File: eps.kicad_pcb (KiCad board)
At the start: 4 copper layers, 95.9 x 90.2 mm, 185 parts, among them J1 PC104-8BIT, J2 PC104PTH, J3 PC104PTH, J4 PC104PTH, J5 PC104PTH, P1 3pin-DC-power, P2 3pin-DC-power, Q10 CSD17551Q3A, Q11 CSD17551Q3A, Q12 CSD17551Q3A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

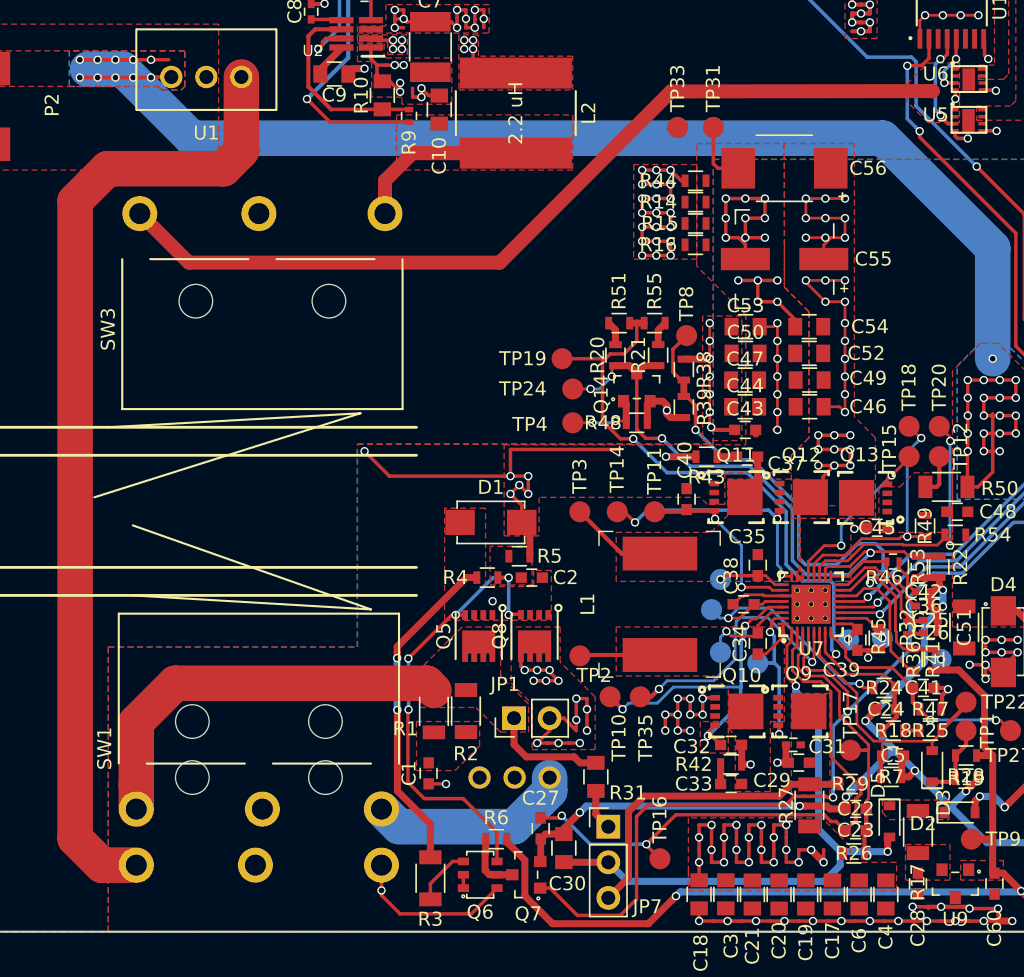
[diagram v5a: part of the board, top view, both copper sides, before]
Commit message: Fix switch footprint terminal spacing and adjust track ends accordingly
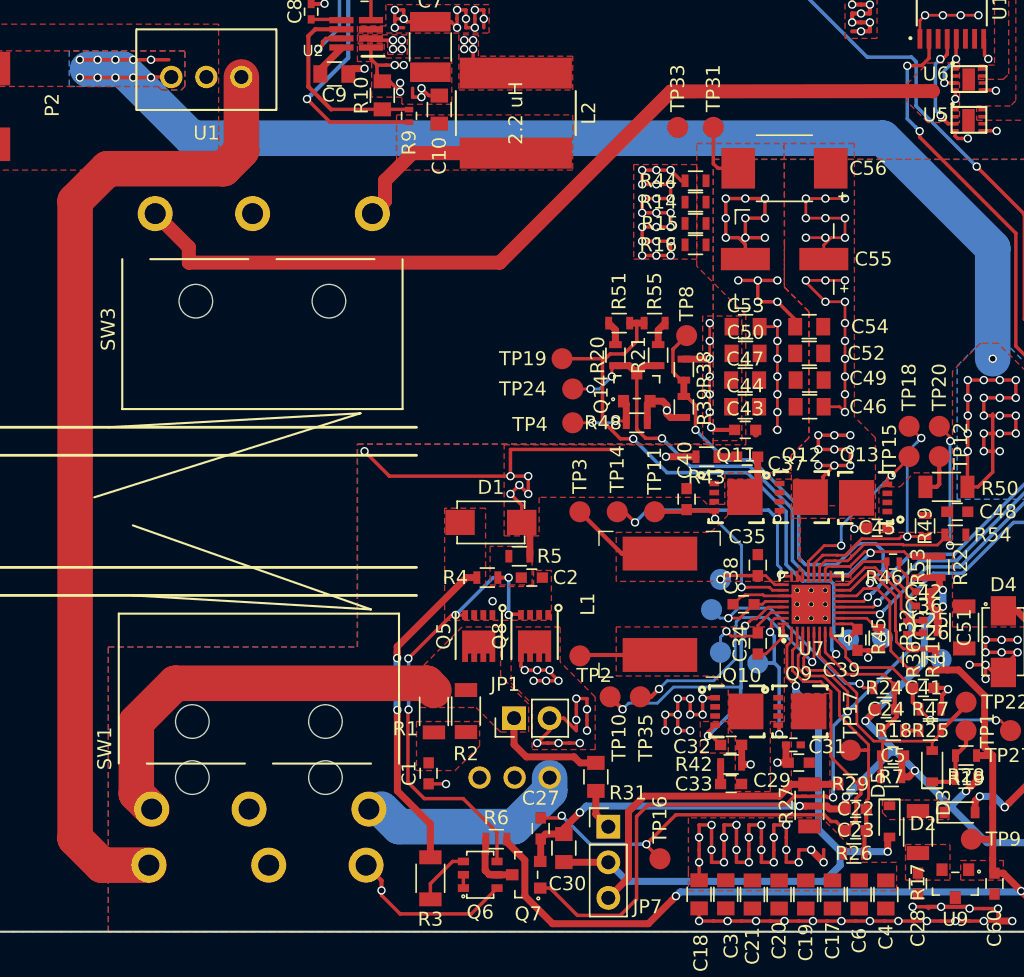
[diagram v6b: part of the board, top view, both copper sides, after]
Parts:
- SW1: footprint SFUSat:SS-3GLPD-L -> SS-3GLPD-L
- SW3: footprint SFUSat:SS-3GLPD-R -> SS-3GLPD-R
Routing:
- net GNDPWR: track 151.5 -> 150.2 mm
- net /return: track 69.3 -> 70.2 mm

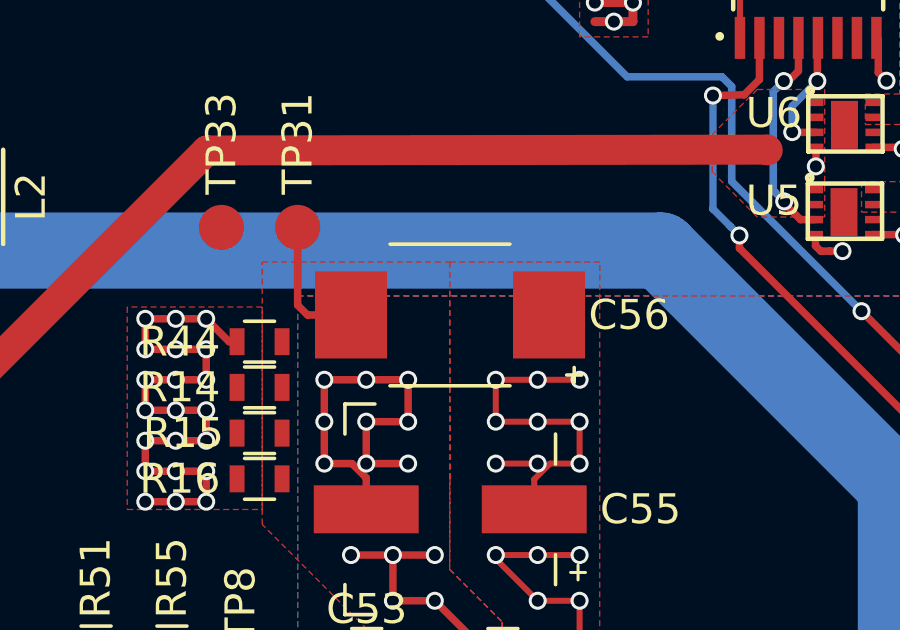
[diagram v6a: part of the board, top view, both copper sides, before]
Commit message: Move pads closer together on C56 footprint
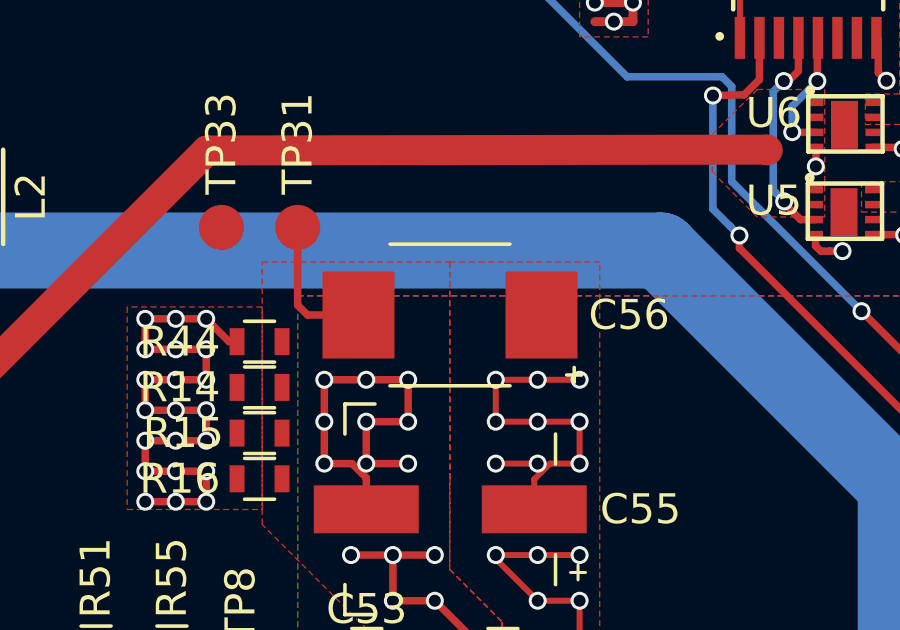
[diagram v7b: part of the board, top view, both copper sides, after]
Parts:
- C56: footprint SFUSat-cap:C_TANT_2917 -> C_TANT_2917
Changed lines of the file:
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@@
     (uvia_drill 0.1)
+  )
+  (module C_TANT_2917 (layer F.Cu)
+    (at 169.26 80.517 180)
+    (fp_text reference C56 (at -5.971 0 180) (layer F.SilkS)
+      (effects (font (size 1 1) (thickness 0.15)))
+    )
+    (fp_text value 47u (at 0 3.5 180) (layer F.Fab)
+      (effects (font (size 1 1) (thickness 0.15)))
+    )
+    (fp_text user REF** (at 0 -3.5 180) (layer F.Fab)
+      (effects (font (size 1 1) (thickness 0.15)))
+    )
+    (fp_line (start 4.525 2.435) (end 4.525 -2.435) (layer F.CrtYd) (width 0.05))
+    (fp_line (start 4.525 -2.435) (end -4.525 -2.435) (layer F.CrtYd) (width 0.05))
+    (fp_line (start -4.525 -2.435) (end -4.525 2.435) (layer F.CrtYd) (width 0.05))
+    (fp_line (start -4.525 2.435) (end 4.525 2.435) (layer F.CrtYd) (width 0.05))
+    (fp_line (start -4.14 -2.25) (end -4.14 -1.75) (layer F.SilkS) (width 0.12))
+    (fp_line (start -3.89 -2) (end -4.39 -2) (layer F.SilkS) (width 0.12))
+    (fp_line (start -2 2.36) (end 2 2.36) (layer F.SilkS) (width 0.12))
+    (fp_line (start -2 -2.36) (end 2 -2.36) (layer F.SilkS) (width 0.12))
+    (fp_line (start -3.75 -2.25) (end -3.75 2.25) (layer F.Fab) (width 0.1))
+    (fp_line (start -3.75 2.25) (end 3.75 2.25) (layer F.Fab) (width 0.1))
+    (fp_line (start 3.75 2.25) (end 3.75 -2.25) (layer F.Fab) (width 0.1))
+    (fp_line (start 3.75 -2.25) (end -3.75 -2.25) (layer F.Fab) (width 0.1))
+    (pad 1 smd rect (at -3.05 0 180) (size 2.4 2.9) (layers F.Cu F.Paste F.Mask)
+      (net 104 /VSYS_UP))
+    (pad 2 smd rect (at 3.05 0 180) (size 2.4 2.9) (layers F.Cu F.Paste F.Mask)
+      (net 44 GNDPWR))
   )
   (module SFUSat:SS-3GLPD-L (layer B.Cu)
@@
     )
   )
-  (module SFUSat-cap:C_TANT_2917 (layer F.Cu)
-    (at 169.26 80.517 180)
-    (fp_text reference C56 (at -5.971 0 180) (layer F.SilkS)
-      (effects (font (size 1 1) (thickness 0.15)))
-    )
-    (fp_text value 47u (at 0 3.5 180) (layer F.Fab)
-      (effects (font (size 1 1) (thickness 0.15)))
-    )
-    (fp_text user REF** (at 0 -3.5 180) (layer F.Fab)
-      (effects (font (size 1 1) (thickness 0.15)))
-    )
-    (fp_line (start 4.525 2.435) (end 4.525 -2.435) (layer F.CrtYd) (width 0.05))
-    (fp_line (start 4.525 -2.435) (end -4.525 -2.435) (layer F.CrtYd) (width 0.05))
-    (fp_line (start -4.525 -2.435) (end -4.525 2.435) (layer F.CrtYd) (width 0.05))
-    (fp_line (start -4.525 2.435) (end 4.525 2.435) (layer F.CrtYd) (width 0.05))
-    (fp_line (start -4.14 -2.25) (end -4.14 -1.75) (layer F.SilkS) (width 0.12))
-    (fp_line (start -3.89 -2) (end -4.39 -2) (layer F.SilkS) (width 0.12))
-    (fp_line (start -2 2.36) (end 2 2.36) (layer F.SilkS) (width 0.12))
-    (fp_line (start -2 -2.36) (end 2 -2.36) (layer F.SilkS) (width 0.12))
-    (fp_line (start -3.75 -2.25) (end -3.75 2.25) (layer F.Fab) (width 0.1))
-    (fp_line (start -3.75 2.25) (end 3.75 2.25) (layer F.Fab) (width 0.1))
-    (fp_line (start 3.75 2.25) (end 3.75 -2.25) (layer F.Fab) (width 0.1))
-    (fp_line (start 3.75 -2.25) (end -3.75 -2.25) (layer F.Fab) (width 0.1))
-    (pad 1 smd rect (at -3.3 0 180) (size 2.4 2.9) (layers F.Cu F.Paste F.Mask)
-      (net 104 /VSYS_UP))
-    (pad 2 smd rect (at 3.3 0 180) (size 2.4 2.9) (layers F.Cu F.Paste F.Mask)
-      (net 44 GNDPWR))
-  )
   (module SFUSat:B3B-XH-A (layer F.Cu)

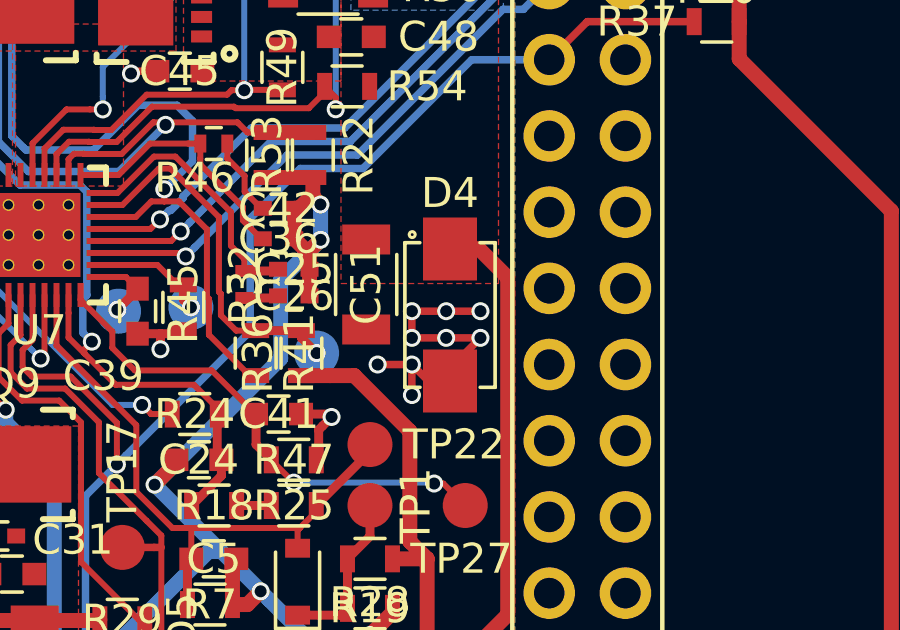
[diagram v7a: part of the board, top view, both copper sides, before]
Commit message: Update D4 pad dimensions and spacing to patch datasheet, regenerate pours
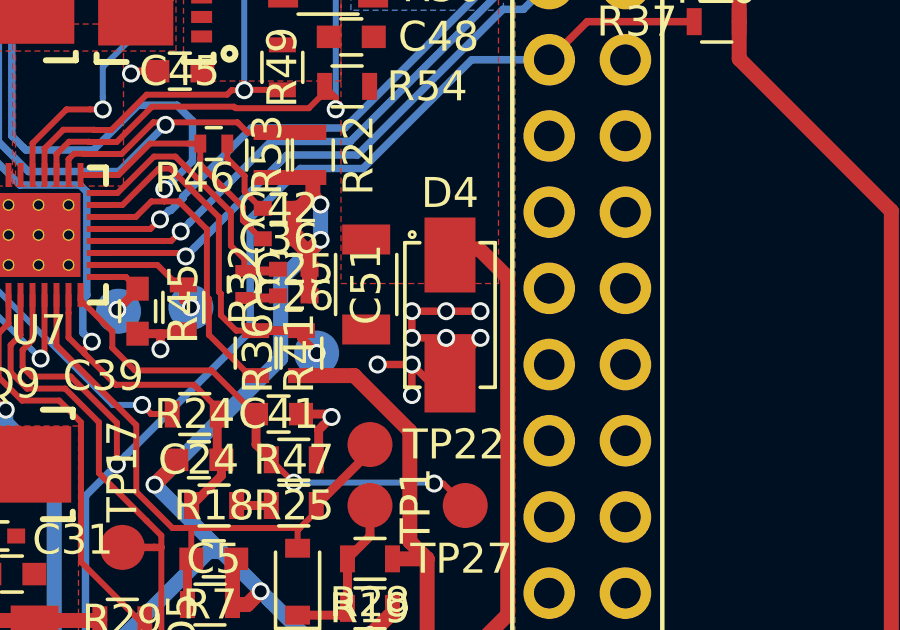
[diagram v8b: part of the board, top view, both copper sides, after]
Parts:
- D4: footprint SFUSat:DO-214AC -> DO-214AC
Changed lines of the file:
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@@
     (31 B.Cu signal hide)
     (33 F.Adhes user hide)
-    (35 F.Paste user hide)
+    (35 F.Paste user)
     (36 B.SilkS user)
     (37 F.SilkS user)
     (38 B.Mask user)
     (39 F.Mask user)
-    (40 Dwgs.User user hide)
-    (41 Cmts.User user hide)
+    (40 Dwgs.User user)
+    (41 Cmts.User user)
     (42 Eco1.User user hide)
-    (43 Eco2.User user hide)
+    (43 Eco2.User user)
     (44 Edge.Cuts user)
     (45 Margin user hide)
@@
     (uvia_drill 0.1)
   )
+  (module DO-214AC (layer F.Cu)
+    (at 184.883 114.299 90)
+    (fp_text reference D4 (at 4.064 0 180) (layer F.SilkS)
+      (effects (font (size 1 1) (thickness 0.15)))
+    )
+    (fp_text value DNP (at 0 2.5 90) (layer F.Fab)
+      (effects (font (size 1 1) (thickness 0.15)))
+    )
+    (fp_circle (center 2.08 -1.18) (end 2.13 -1.18) (layer F.Fab) (width 0.2))
+    (fp_circle (center 2.68 -1.26) (end 2.73 -1.26) (layer F.SilkS) (width 0.2))
+    (fp_text user REF** (at 0 -2.5 90) (layer F.Fab)
+      (effects (font (size 1 1) (thickness 0.15)))
+    )
+    (fp_line (start -3.275 -1.59) (end -3.275 1.59) (layer F.CrtYd) (width 0.05))
+    (fp_line (start -3.275 1.59) (end 3.275 1.59) (layer F.CrtYd) (width 0.05))
+    (fp_line (start 3.275 1.59) (end 3.275 -1.59) (layer F.CrtYd) (width 0.05))
+    (fp_line (start 3.275 -1.59) (end -3.275 -1.59) (layer F.CrtYd) (width 0.05))
+    (fp_line (start 2.41 -1.505) (end 2.41 -1.005) (layer F.SilkS) (width 0.12))
+    (fp_line (start -2.41 -1.505) (end 2.41 -1.505) (layer F.SilkS) (width 0.12))
+    (fp_line (start 2.41 1) (end 2.41 1.505) (layer F.SilkS) (width 0.12))
+    (fp_line (start 2.41 1.505) (end -2.41 1.505) (layer F.SilkS) (width 0.12))
+    (fp_line (start -2.41 1.505) (end -2.41 1.005) (layer F.SilkS) (width 0.12))
+    (fp_line (start -2.41 -1) (end -2.41 -1.505) (layer F.SilkS) (width 0.12))
+    (fp_line (start -2.3 -1.395) (end 2.3 -1.395) (layer F.Fab) (width 0.1))
+    (fp_line (start 2.3 -1.395) (end 2.3 1.395) (layer F.Fab) (width 0.1))
+    (fp_line (start 2.3 1.395) (end -2.3 1.395) (layer F.Fab) (width 0.1))
+    (fp_line (start -2.3 1.395) (end -2.3 -1.395) (layer F.Fab) (width 0.1))
+    (pad 1 smd rect (at -2 0 90) (size 2.5 1.7) (layers F.Cu F.Paste F.Mask)
+      (net 44 GNDPWR))
+    (pad 2 smd rect (at 2 0 90) (size 2.5 1.7) (layers F.Cu F.Paste F.Mask)
+      (net 97 /pack+))
+  )
   (module C_TANT_2917 (layer F.Cu)
     (at 169.26 80.517 180)
@@
       (net 44 GNDPWR))
   )
-  (module SFUSat:DO-214AC (layer F.Cu)
-    (at 184.883 114.299 90)
-    (fp_text reference D4 (at 4.064 0 180) (layer F.SilkS)
-      (effects (font (size 1 1) (thickness 0.15)))
-    )
-    (fp_text value DNP (at 0 2.5 90) (layer F.Fab)
-      (effects (font (size 1 1) (thickness 0.15)))
-    )
-    (fp_circle (center 2.08 -1.18) (end 2.13 -1.18) (layer F.Fab) (width 0.2))
-    (fp_circle (center 2.68 -1.26) (end 2.73 -1.26) (layer F.SilkS) (width 0.2))
-    (fp_text user REF** (at 0 -2.5 90) (layer F.Fab)
-      (effects (font (size 1 1) (thickness 0.15)))
-    )
-    (fp_line (start -3.275 -1.59) (end -3.275 1.59) (layer F.CrtYd) (width 0.05))
-    (fp_line (start -3.275 1.59) (end 3.275 1.59) (layer F.CrtYd) (width 0.05))
-    (fp_line (start 3.275 1.59) (end 3.275 -1.59) (layer F.CrtYd) (width 0.05))
-    (fp_line (start 3.275 -1.59) (end -3.275 -1.59) (layer F.CrtYd) (width 0.05))
-    (fp_line (start 2.41 -1.505) (end 2.41 -1.005) (layer F.SilkS) (width 0.12))
-    (fp_line (start -2.41 -1.505) (end 2.41 -1.505) (layer F.SilkS) (width 0.12))
-    (fp_line (start 2.41 1) (end 2.41 1.505) (layer F.SilkS) (width 0.12))
-    (fp_line (start 2.41 1.505) (end -2.41 1.505) (layer F.SilkS) (width 0.12))
-    (fp_line (start -2.41 1.505) (end -2.41 1.005) (layer F.SilkS) (width 0.12))
-    (fp_line (start -2.41 -1) (end -2.41 -1.505) (layer F.SilkS) (width 0.12))
-    (fp_line (start -2.3 -1.395) (end 2.3 -1.395) (layer F.Fab) (width 0.1))
-    (fp_line (start 2.3 -1.395) (end 2.3 1.395) (layer F.Fab) (width 0.1))
-    (fp_line (start 2.3 1.395) (end -2.3 1.395) (layer F.Fab) (width 0.1))
-    (fp_line (start -2.3 1.395) (end -2.3 -1.395) (layer F.Fab) (width 0.1))
-    (pad 1 smd rect (at -2.2 0 90) (size 2.1 1.8) (layers F.Cu F.Paste F.Mask)
-      (net 44 GNDPWR))
-    (pad 2 smd rect (at 2.2 0 90) (size 2.1 1.8) (layers F.Cu F.Paste F.Mask)
-      (net 97 /pack+))
-  )
   (module SFUSat-ind:L_8030 (layer F.Cu)
     (at 160.372 111.632 90)
@@
   (segment (start 130.6106 58.9982) (end 131.0606 58.9982) (width 0.5) (layer F.Cu) (net 42))
   (segment (start 131.0606 58.9982) (end 131.6606 58.9982) (width 0.5) (layer F.Cu) (net 42))
+  (segment (start 140.5 131.35) (end 139.4 130.25) (width 0.3) (layer F.Cu) (net 44))
   (segment (start 140.5 132.0536) (end 140.5 131.35) (width 0.3) (layer F.Cu) (net 44))
   (segment (start 146.91 133.73) (end 141.83 133.73) (width 0.25) (layer F.Cu) (net 44))
@@
   (via (at 140.5 132.0536) (size 0.6) (drill 0.4) (layers F.Cu B.Cu) (net 44))
   (segment (start 140.5 132.4) (end 140.5 132.0536) (width 0.25) (layer F.Cu) (net 44))
-  (segment (start 140.5 131.35) (end 139.4 130.25) (width 0.3) (layer F.Cu) (net 44) (status 800000))
   (segment (start 143.862 124.447) (end 145.0946 124.447) (width 0.25) (layer F.Cu) (net 44))
   (segment (start 145.0946 124.447) (end 145.1066 124.459) (width 0.25) (layer F.Cu) (net 44))
@@
   (segment (start 185.278755 125.819449) (end 184.978756 126.119448) (width 0.5) (layer F.Cu) (net 97))
   (via (at 184.978756 126.119448) (size 0.6) (drill 0.4) (layers F.Cu B.Cu) (net 97))
-  (segment (start 123.9 130.25) (end 120.542868 130.25) (width 2.54) (layer F.Cu) (net 98) (status 400000))
+  (segment (start 123.9 130.25) (end 120.542868 130.25) (width 2.54) (layer F.Cu) (net 98))
   (segment (start 130.5 79.22) (end 130.527 79.247) (width 0.781) (layer F.Cu) (net 98))
   (segment (start 130.527 79.247) (end 129.228272 80.545728) (width 2.54) (layer F.Cu) (net 98))
@@
   (via (at 145.894 70.484) (size 0.6) (drill 0.4) (layers F.Cu B.Cu) (net 102))
   (segment (start 113 60.9) (end 113 61.5) (width 0.781) (layer F.Cu) (net 102))
+  (segment (start 140.75 82.85) (end 139.85 83.75) (width 1) (layer F.Cu) (net 103))
   (segment (start 140.75 81.395937) (end 140.75 82.85) (width 1) (layer F.Cu) (net 103))
   (segment (start 142.708437 79.4375) (end 140.75 81.395937) (width 1) (layer F.Cu) (net 103))
   (segment (start 150.085 79.4375) (end 142.708437 79.4375) (width 1) (layer F.Cu) (net 103))
-  (segment (start 140.75 82.85) (end 139.85 83.75) (width 1) (layer F.Cu) (net 103) (status 800000))
   (segment (start 135.482656 75.872971) (end 135.182657 75.572972) (width 0.25) (layer F.Cu) (net 103))
   (segment (start 136.835685 77.226) (end 135.482656 75.872971) (width 0.25) (layer F.Cu) (net 103))
@@
   (segment (start 189.46 104.52) (end 188.19 105.79) (width 0.25) (layer F.Cu) (net 112))
   (via (at 173.780299 119.281926) (size 0.6) (drill 0.4) (layers F.Cu B.Cu) (net 112))
-  (segment (start 126.748 87.248) (end 126.748 86.148) (width 1) (layer F.Cu) (net 115))
   (segment (start 126.748 87.248) (end 148.942 87.248) (width 1) (layer F.Cu) (net 115))
   (segment (start 148.942 87.248) (end 161.157977 75.032023) (width 1) (layer F.Cu) (net 115))
   (segment (start 161.157977 75.032023) (end 179.8284 75.0052) (width 1) (layer F.Cu) (net 115))
   (segment (start 179.852377 75.029177) (end 179.8284 75.0052) (width 1) (layer F.Cu) (net 115))
-  (segment (start 126.748 86.148) (end 124.35 83.75) (width 1) (layer F.Cu) (net 115) (status 800000))
+  (segment (start 126.748 86.148) (end 124.35 83.75) (width 1) (layer F.Cu) (net 115))
+  (segment (start 126.748 87.248) (end 126.748 86.148) (width 1) (layer F.Cu) (net 115))
   (segment (start 157.197 98.551) (end 157.844 98.551) (width 0.2) (layer F.Cu) (net 116))
   (segment (start 157.844 98.551) (end 157.971 98.678) (width 0.2) (layer F.Cu) (net 116))
@@
   (segment (start 180.6666 74.421) (end 180.6666 73.5574) (width 0.25) (layer B.Cu) (net 119))
   (segment (start 181.5048 71.2992) (end 181.525 71.279) (width 0.25) (layer F.Cu) (net 119))
+  (segment (start 123 125.15) (end 124.1 126.25) (width 2.54) (layer F.Cu) (net 129))
   (segment (start 123 120.048398) (end 123 125.15) (width 2.54) (layer F.Cu) (net 129))
   (segment (start 143.73648 117.26948) (end 125.778918 117.26948) (width 2.54) (layer F.Cu) (net 129))
   (segment (start 144.243 117.776) (end 143.73648 117.26948) (width 2.54) (layer F.Cu) (net 129))
   (segment (start 125.778918 117.26948) (end 123 120.048398) (width 2.54) (layer F.Cu) (net 129))
-  (segment (start 123 125.15) (end 124.1 126.25) (width 2.54) (layer F.Cu) (net 129) (status 800000))
   (segment (start 123 126.25) (end 123 126.3) (width 0.781) (layer F.Cu) (net 129))
   (segment (start 155.8 122.951) (end 154.675 122.951) (width 0.5) (layer F.Cu) (net 129))
